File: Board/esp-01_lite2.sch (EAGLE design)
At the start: 26 parts, among them IC1 TINY13-20SU

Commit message: update board
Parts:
- added R9: 3k3, rcl:R-EU_R0805
- R10: value 3k3 -> 0
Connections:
- net GND: now also R9.2
- net IN1: now also C6.2, R6.2; no longer C5.2, R1.2
- net IN2: now also C5.2, R1.2; no longer C6.2, R6.2
- net N$3: now also X3.-3; no longer X3.-1
- net N$4: now also X3.-1; no longer X3.-3
- net WAKE_UP: now also R9.1
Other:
- moved on the sheet: C5, R1, X3
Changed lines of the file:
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@@
 <?xml version="1.0" encoding="utf-8"?>
 <!DOCTYPE eagle SYSTEM "eagle.dtd">
-<eagle version="9.0.0">
+<eagle version="8.7.0">
 <drawing>
 <settings>
@@
 <setting verticaltext="up"/>
 </settings>
-<grid distance="0.01" unitdist="inch" unit="inch" style="lines" multiple="1" display="no" altdistance="0.01" altunitdist="inch" altunit="inch"/>
+<grid distance="0.1" unitdist="inch" unit="inch" style="lines" multiple="1" display="no" altdistance="0.01" altunitdist="inch" altunit="inch"/>
 <layers>
 <layer number="1" name="Top" color="4" fill="1" visible="no" active="no"/>
@@
 <part name="GND3" library="supply1" deviceset="GND" device=""/>
 <part name="GND4" library="supply1" deviceset="GND" device=""/>
-<part name="R10" library="resistor" library_urn="urn:adsk.eagle:library:348" deviceset="R-EU_" device="M0805" package3d_urn="urn:adsk.eagle:package:26079/1" value="3k3"/>
+<part name="R10" library="resistor" library_urn="urn:adsk.eagle:library:348" deviceset="R-EU_" device="M0805" package3d_urn="urn:adsk.eagle:package:26079/1" value="0"/>
 <part name="GND6" library="supply1" deviceset="GND" device=""/>
 <part name="R11" library="rcl" deviceset="R-EU_" device="R0805" value="200">
@@
 <part name="X3" library="con-wago255" library_urn="urn:adsk.eagle:library:198" deviceset="233-104" device="" package3d_urn="urn:adsk.eagle:package:10915/1"/>
 <part name="U$2" library="MCP1700T-3302E_TT" deviceset="MCP1700T-3302E/TT" device=""/>
+<part name="R9" library="rcl" deviceset="R-EU_" device="R0805" value="3k3">
+<attribute name="OM" value="3k6"/>
+</part>
+<part name="GND2" library="supply1" deviceset="GND" device=""/>
 </parts>
 <sheets>
@@
 </instance>
 <instance part="R8" gate="G$1" x="120.904" y="56.896" rot="R270"/>
-<instance part="R1" gate="G$1" x="131.826" y="82.804" smashed="yes">
-<attribute name="NAME" x="130.556" y="84.3026" size="1.778" layer="95"/>
-<attribute name="VALUE" x="130.556" y="79.502" size="1.778" layer="96"/>
+<instance part="R1" gate="G$1" x="131.826" y="92.964" smashed="yes">
+<attribute name="NAME" x="130.556" y="94.4626" size="1.778" layer="95"/>
+<attribute name="VALUE" x="130.556" y="89.662" size="1.778" layer="96"/>
 </instance>
 <instance part="R6" gate="G$1" x="131.826" y="115.824" smashed="yes">
@@
 <attribute name="VALUE" x="130.556" y="112.522" size="1.778" layer="96"/>
 </instance>
-<instance part="C5" gate="G$1" x="136.906" y="92.964" smashed="yes">
-<attribute name="NAME" x="139.954" y="90.551" size="1.778" layer="95"/>
-<attribute name="VALUE" x="129.54" y="90.297" size="1.778" layer="96"/>
+<instance part="C5" gate="G$1" x="136.906" y="101.092" smashed="yes">
+<attribute name="NAME" x="139.954" y="98.679" size="1.778" layer="95"/>
+<attribute name="VALUE" x="129.54" y="98.425" size="1.778" layer="96"/>
 </instance>
 <instance part="C6" gate="G$1" x="136.906" y="108.204" smashed="yes" rot="R180">
@@
 </instance>
 <instance part="S2" gate="1" x="87.376" y="38.354"/>
-<instance part="X3" gate="G$1" x="99.314" y="106.68" rot="R180"/>
+<instance part="X3" gate="G$1" x="105.918" y="105.664" rot="R180"/>
 <instance part="U$2" gate="G$1" x="46.736" y="115.316" rot="R180"/>
+<instance part="R9" gate="G$1" x="42.164" y="26.162" smashed="yes" rot="R270">
+<attribute name="NAME" x="36.8046" y="24.384" size="1.778" layer="95"/>
+<attribute name="VALUE" x="36.576" y="27.178" size="1.778" layer="96"/>
+</instance>
+<instance part="GND2" gate="1" x="42.164" y="15.494"/>
 </instances>
 <busses>
@@
 <wire x1="150.876" y1="105.664" x2="150.876" y2="103.124" width="0.1524" layer="91"/>
 </segment>
+<segment>
+<pinref part="R9" gate="G$1" pin="2"/>
+<wire x1="42.164" y1="21.082" x2="42.164" y2="18.034" width="0.1524" layer="91"/>
+<pinref part="GND2" gate="1" pin="GND"/>
+</segment>
 </net>
 <net name="+3V3" class="0">
@@
 </segment>
 <segment>
+<pinref part="R1" gate="G$1" pin="2"/>
+<pinref part="C5" gate="G$1" pin="2"/>
+<wire x1="136.906" y1="96.012" x2="136.906" y2="92.964" width="0.1524" layer="91"/>
+<wire x1="136.906" y1="92.964" x2="146.05" y2="92.964" width="0.1524" layer="91"/>
+<junction x="136.906" y="92.964"/>
+<label x="146.812" y="92.71" size="1.778" layer="95"/>
+</segment>
+</net>
+<net name="IN1" class="0">
+<segment>
+<pinref part="IC1" gate="G$1" pin="PB3/PCINT3/CLKI/ADC3"/>
+<wire x1="128.778" y1="41.656" x2="112.268" y2="41.656" width="0.1524" layer="91"/>
+<label x="112.014" y="41.91" size="1.778" layer="95"/>
+</segment>
+<segment>
 <pinref part="R6" gate="G$1" pin="2"/>
 <pinref part="C6" gate="G$1" pin="2"/>
@@
 <wire x1="136.906" y1="115.824" x2="144.526" y2="115.824" width="0.1524" layer="91"/>
 <junction x="136.906" y="115.824"/>
-<label x="144.526" y="115.824" size="1.778" layer="95"/>
-</segment>
-</net>
-<net name="IN1" class="0">
-<segment>
-<pinref part="IC1" gate="G$1" pin="PB3/PCINT3/CLKI/ADC3"/>
-<wire x1="128.778" y1="41.656" x2="112.268" y2="41.656" width="0.1524" layer="91"/>
-<label x="112.014" y="41.91" size="1.778" layer="95"/>
-</segment>
-<segment>
-<pinref part="R1" gate="G$1" pin="2"/>
-<pinref part="C5" gate="G$1" pin="2"/>
-<wire x1="136.906" y1="87.884" x2="136.906" y2="82.804" width="0.1524" layer="91"/>
-<wire x1="136.906" y1="82.804" x2="144.526" y2="82.804" width="0.1524" layer="91"/>
-<junction x="136.906" y="82.804"/>
-<label x="144.526" y="82.804" size="1.778" layer="95"/>
+<label x="145.288" y="116.332" size="1.778" layer="95"/>
 </segment>
 </net>
@@
 <segment>
 <pinref part="C5" gate="G$1" pin="1"/>
-<wire x1="123.19" y1="95.504" x2="136.906" y2="95.504" width="0.1524" layer="91"/>
 <pinref part="C6" gate="G$1" pin="1"/>
 <wire x1="124.206" y1="105.664" x2="136.906" y2="105.664" width="0.1524" layer="91"/>
 <wire x1="139.192" y1="105.664" x2="136.906" y2="105.664" width="0.1524" layer="91"/>
 <junction x="136.906" y="105.664"/>
-<wire x1="136.906" y1="105.664" x2="136.906" y2="95.504" width="0.1524" layer="91"/>
-<junction x="136.906" y="95.504"/>
-<label x="137.668" y="99.06" size="1.778" layer="95"/>
+<wire x1="136.906" y1="105.664" x2="136.906" y2="103.632" width="0.1524" layer="91"/>
+<label x="120.904" y="103.124" size="1.778" layer="95"/>
 <pinref part="R10" gate="G$1" pin="1"/>
+<wire x1="124.206" y1="105.664" x2="124.206" y2="110.744" width="0.1524" layer="91"/>
+<wire x1="124.206" y1="110.744" x2="113.538" y2="110.744" width="0.1524" layer="91"/>
+<pinref part="X3" gate="G$1" pin="-4"/>
 <pinref part="X3" gate="G$1" pin="-2"/>
-<wire x1="123.19" y1="95.504" x2="123.19" y2="106.68" width="0.1524" layer="91"/>
-<wire x1="123.19" y1="106.68" x2="106.934" y2="106.68" width="0.1524" layer="91"/>
-<wire x1="124.206" y1="105.664" x2="124.206" y2="111.76" width="0.1524" layer="91"/>
-<wire x1="124.206" y1="111.76" x2="106.934" y2="111.76" width="0.1524" layer="91"/>
-<pinref part="X3" gate="G$1" pin="-4"/>
+<wire x1="124.206" y1="105.664" x2="113.538" y2="105.664" width="0.1524" layer="91"/>
+<junction x="124.206" y="105.664"/>
 </segment>
 <segment>
@@
 <segment>
 <pinref part="U$1" gate="G$1" pin="CH_PD"/>
-<wire x1="18.034" y1="46.736" x2="43.942" y2="46.736" width="0.1524" layer="91"/>
+<wire x1="18.034" y1="46.736" x2="42.164" y2="46.736" width="0.1524" layer="91"/>
 <label x="18.034" y="47.498" size="1.778" layer="95"/>
+<pinref part="R9" gate="G$1" pin="1"/>
+<wire x1="42.164" y1="46.736" x2="43.942" y2="46.736" width="0.1524" layer="91"/>
+<wire x1="42.164" y1="31.242" x2="42.164" y2="46.736" width="0.1524" layer="91"/>
+<junction x="42.164" y="46.736"/>
 </segment>
 </net>
@@
 <pinref part="R6" gate="G$1" pin="1"/>
 <wire x1="126.746" y1="115.824" x2="116.84" y2="115.824" width="0.1524" layer="91"/>
-<pinref part="X3" gate="G$1" pin="-1"/>
-<wire x1="106.934" y1="104.14" x2="116.84" y2="104.14" width="0.1524" layer="91"/>
-<wire x1="116.84" y1="104.14" x2="116.84" y2="115.824" width="0.1524" layer="91"/>
+<pinref part="X3" gate="G$1" pin="-3"/>
+<wire x1="113.538" y1="108.204" x2="116.84" y2="108.204" width="0.1524" layer="91"/>
+<wire x1="116.84" y1="108.204" x2="116.84" y2="115.824" width="0.1524" layer="91"/>
 </segment>
 </net>
@@
 </segment>
 </net>
-<net name="N$4" class="0">
-<segment>
-<wire x1="126.746" y1="91.44" x2="126.746" y2="82.804" width="0.1524" layer="91"/>
-<pinref part="R1" gate="G$1" pin="1"/>
-<pinref part="X3" gate="G$1" pin="-3"/>
-<wire x1="106.934" y1="109.22" x2="120.396" y2="109.22" width="0.1524" layer="91"/>
-<wire x1="120.396" y1="109.22" x2="120.396" y2="91.44" width="0.1524" layer="91"/>
-<wire x1="120.396" y1="91.44" x2="126.746" y2="91.44" width="0.1524" layer="91"/>
-</segment>
-</net>
 <net name="N$2" class="0">
 <segment>
@@
 </segment>
 </net>
+<net name="N$4" class="0">
+<segment>
+<pinref part="X3" gate="G$1" pin="-1"/>
+<wire x1="113.538" y1="103.124" x2="116.84" y2="103.124" width="0.1524" layer="91"/>
+<wire x1="116.84" y1="103.124" x2="116.84" y2="92.964" width="0.1524" layer="91"/>
+<pinref part="R1" gate="G$1" pin="1"/>
+<wire x1="116.84" y1="92.964" x2="126.746" y2="92.964" width="0.1524" layer="91"/>
+</segment>
+</net>

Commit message: board
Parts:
- R11, R4: value 200 -> 300
- R8: device rcl:R-EU_0204/5 -> rcl:R-EU_R0805
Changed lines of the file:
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@@
 <part name="+3V3" library="supply1" deviceset="+3V3" device=""/>
 <part name="+3V4" library="supply1" deviceset="+3V3" device=""/>
-<part name="R4" library="rcl" library_urn="urn:adsk.eagle:library:334" deviceset="R-EU_" device="0207/2V" package3d_urn="urn:adsk.eagle:package:23490/1" value="200">
+<part name="R4" library="rcl" library_urn="urn:adsk.eagle:library:334" deviceset="R-EU_" device="0207/2V" package3d_urn="urn:adsk.eagle:package:23490/1" value="300">
 <spice>
 <pinmapping spiceprefix="R">
@@
 <part name="LOG" library="pinhead" deviceset="PINHD-1X1" device="" value="LOG"/>
 <part name="+3V8" library="supply1" deviceset="+3V3" device=""/>
-<part name="R8" library="rcl" library_urn="urn:adsk.eagle:library:334" deviceset="R-EU_" device="0204/5" package3d_urn="urn:adsk.eagle:package:23488/1" value="3k3">
+<part name="R8" library="rcl" library_urn="urn:adsk.eagle:library:334" deviceset="R-EU_" device="R0805" package3d_urn="urn:adsk.eagle:package:23553/2" value="3k3">
 <spice>
 <pinmapping spiceprefix="C">
@@
 <part name="R10" library="resistor" library_urn="urn:adsk.eagle:library:348" deviceset="R-EU_" device="M0805" package3d_urn="urn:adsk.eagle:package:26079/1" value="0"/>
 <part name="GND6" library="supply1" deviceset="GND" device=""/>
-<part name="R11" library="rcl" deviceset="R-EU_" device="R0805" value="200">
+<part name="R11" library="rcl" deviceset="R-EU_" device="R0805" value="300">
 <attribute name="OM" value="3k6"/>
 </part>

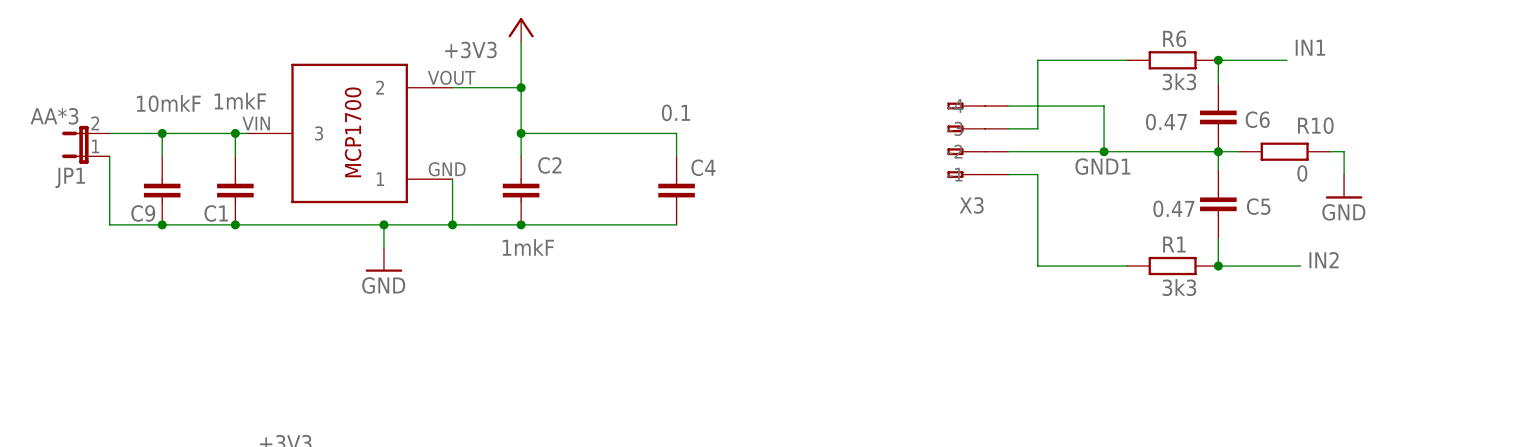
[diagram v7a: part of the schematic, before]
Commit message: v0.4 remove capacitor
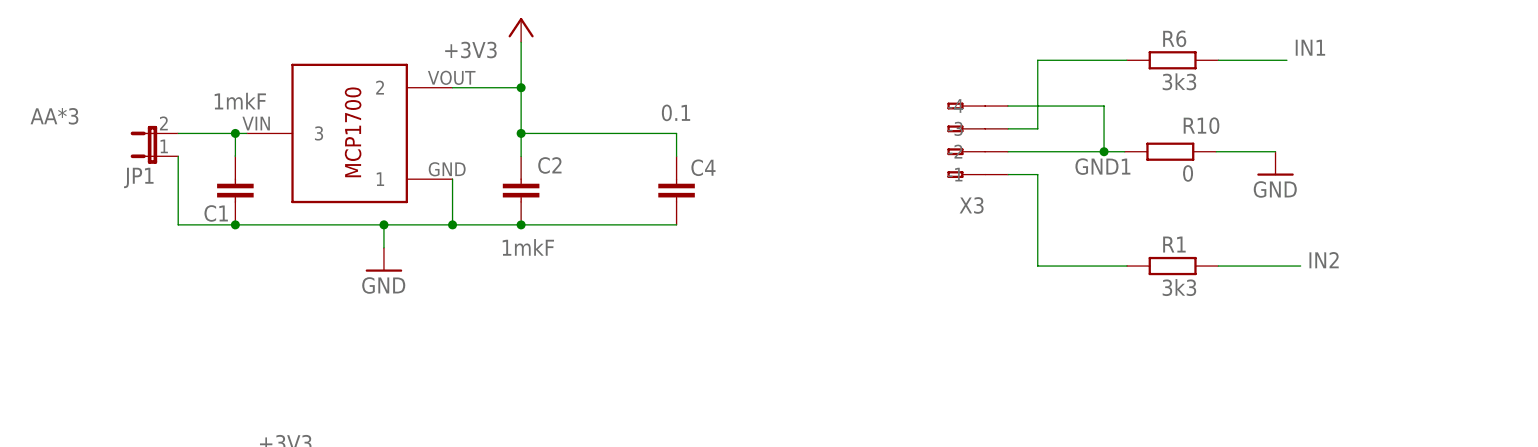
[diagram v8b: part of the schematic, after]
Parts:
- removed C5, C6: 0.47, resistor:C-EUC0805
- removed C9: 10mkF, rcl:C-EU025-030X050
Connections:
- net AA*3: no longer C9.1
- net GND: no longer C9.2
- net GND1: no longer C5.1, C6.1
- net IN1: no longer C6.2
- net IN2: no longer C5.2
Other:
- moved on the sheet: JP1, R10
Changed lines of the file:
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@@
 </part>
 <part name="R6" library="resistor" library_urn="urn:adsk.eagle:library:348" deviceset="R-EU_" device="M0805" package3d_urn="urn:adsk.eagle:package:26079/1" value="3k3"/>
-<part name="C5" library="resistor" library_urn="urn:adsk.eagle:library:348" deviceset="C-EU" device="C0805" package3d_urn="urn:adsk.eagle:package:26137/1" value="0.47">
-<attribute name="SPICEPREFIX" value="C"/>
-</part>
-<part name="C6" library="resistor" library_urn="urn:adsk.eagle:library:348" deviceset="C-EU" device="C0805" package3d_urn="urn:adsk.eagle:package:26137/1" value="0.47"/>
 <part name="C1" library="resistor" library_urn="urn:adsk.eagle:library:348" deviceset="C-EU" device="C0805" package3d_urn="urn:adsk.eagle:package:26137/1" value="1mkF"/>
 <part name="C2" library="resistor" library_urn="urn:adsk.eagle:library:348" deviceset="C-EU" device="C0805" package3d_urn="urn:adsk.eagle:package:26137/1" value="1mkF"/>
@@
 <attribute name="OM" value="3k6"/>
 </part>
-<part name="C9" library="rcl" library_urn="urn:adsk.eagle:library:334" deviceset="C-EU" device="025-030X050" package3d_urn="urn:adsk.eagle:package:23631/1" value="10mkF"/>
 <part name="GND3" library="supply1" deviceset="GND" device=""/>
 <part name="GND4" library="supply1" deviceset="GND" device=""/>
@@
 <attribute name="VALUE" x="130.556" y="112.522" size="1.778" layer="96"/>
 </instance>
-<instance part="C5" gate="G$1" x="136.906" y="101.092" smashed="yes">
-<attribute name="NAME" x="139.954" y="98.679" size="1.778" layer="95"/>
-<attribute name="VALUE" x="129.54" y="98.425" size="1.778" layer="96"/>
-</instance>
-<instance part="C6" gate="G$1" x="136.906" y="108.204" smashed="yes" rot="R180">
-<attribute name="NAME" x="142.748" y="110.109" size="1.778" layer="95" rot="R180"/>
-<attribute name="VALUE" x="133.604" y="109.855" size="1.778" layer="96" rot="R180"/>
-</instance>
 <instance part="C1" gate="G$1" x="27.686" y="102.616" smashed="yes">
 <attribute name="NAME" x="24.13" y="97.917" size="1.778" layer="95"/>
@@
 <attribute name="VALUE" x="41.656" y="89.916" size="1.778" layer="96"/>
 </instance>
-<instance part="JP1" gate="A" x="11.176" y="105.156" rot="R90"/>
+<instance part="JP1" gate="A" x="18.796" y="105.156" rot="R90"/>
 <instance part="+3V2" gate="G$1" x="59.436" y="120.396" smashed="yes">
 <attribute name="VALUE" x="56.896" y="117.856" size="1.778" layer="96" rot="R180"/>
@@
 <attribute name="VALUE" x="26.416" y="62.738" size="1.778" layer="96"/>
 </instance>
-<instance part="C9" gate="G$1" x="19.558" y="102.616" smashed="yes">
-<attribute name="NAME" x="16.002" y="97.917" size="1.778" layer="95"/>
-<attribute name="VALUE" x="16.51" y="110.109" size="1.778" layer="96"/>
-</instance>
 <instance part="GND3" gate="1" x="12.446" y="14.732"/>
 <instance part="GND4" gate="1" x="120.904" y="22.606"/>
-<instance part="R10" gate="G$1" x="144.272" y="105.664" smashed="yes">
-<attribute name="NAME" x="145.542" y="107.6706" size="1.778" layer="95"/>
-<attribute name="VALUE" x="145.542" y="102.362" size="1.778" layer="96"/>
-</instance>
-<instance part="GND6" gate="1" x="150.876" y="100.584"/>
+<instance part="R10" gate="G$1" x="131.572" y="105.664" smashed="yes">
+<attribute name="NAME" x="132.842" y="107.6706" size="1.778" layer="95"/>
+<attribute name="VALUE" x="132.842" y="102.362" size="1.778" layer="96"/>
+</instance>
+<instance part="GND6" gate="1" x="143.256" y="103.124"/>
 <instance part="R11" gate="G$1" x="87.376" y="26.67" smashed="yes" rot="R270">
 <attribute name="NAME" x="81.2546" y="26.67" size="1.778" layer="95"/>
@@
 <wire x1="44.196" y1="97.536" x2="27.686" y2="97.536" width="0.1524" layer="91"/>
 <pinref part="JP1" gate="A" pin="1"/>
-<wire x1="13.716" y1="105.156" x2="13.716" y2="97.536" width="0.1524" layer="91"/>
-<wire x1="27.686" y1="97.536" x2="19.558" y2="97.536" width="0.1524" layer="91"/>
-<pinref part="C9" gate="G$1" pin="2"/>
-<wire x1="19.558" y1="97.536" x2="13.716" y2="97.536" width="0.1524" layer="91"/>
-<junction x="19.558" y="97.536"/>
+<wire x1="21.336" y1="105.156" x2="21.336" y2="97.536" width="0.1524" layer="91"/>
+<wire x1="27.686" y1="97.536" x2="21.336" y2="97.536" width="0.1524" layer="91"/>
 <junction x="27.686" y="97.536"/>
 <pinref part="C4" gate="G$1" pin="2"/>
@@
 <segment>
 <pinref part="R10" gate="G$1" pin="2"/>
-<wire x1="149.352" y1="105.664" x2="150.876" y2="105.664" width="0.1524" layer="91"/>
+<wire x1="136.652" y1="105.664" x2="143.256" y2="105.664" width="0.1524" layer="91"/>
 <pinref part="GND6" gate="1" pin="GND"/>
-<wire x1="150.876" y1="105.664" x2="150.876" y2="103.124" width="0.1524" layer="91"/>
 </segment>
 <segment>
@@
 <segment>
 <pinref part="R1" gate="G$1" pin="2"/>
-<pinref part="C5" gate="G$1" pin="2"/>
-<wire x1="136.906" y1="96.012" x2="136.906" y2="92.964" width="0.1524" layer="91"/>
 <wire x1="136.906" y1="92.964" x2="146.05" y2="92.964" width="0.1524" layer="91"/>
-<junction x="136.906" y="92.964"/>
 <label x="146.812" y="92.71" size="1.778" layer="95"/>
 </segment>
@@
 <segment>
 <pinref part="R6" gate="G$1" pin="2"/>
-<pinref part="C6" gate="G$1" pin="2"/>
-<wire x1="136.906" y1="113.284" x2="136.906" y2="115.824" width="0.1524" layer="91"/>
 <wire x1="136.906" y1="115.824" x2="144.526" y2="115.824" width="0.1524" layer="91"/>
-<junction x="136.906" y="115.824"/>
 <label x="145.288" y="116.332" size="1.778" layer="95"/>
 </segment>
@@
 <net name="GND1" class="0">
 <segment>
-<pinref part="C5" gate="G$1" pin="1"/>
-<pinref part="C6" gate="G$1" pin="1"/>
-<wire x1="124.206" y1="105.664" x2="136.906" y2="105.664" width="0.1524" layer="91"/>
-<wire x1="139.192" y1="105.664" x2="136.906" y2="105.664" width="0.1524" layer="91"/>
-<junction x="136.906" y="105.664"/>
-<wire x1="136.906" y1="105.664" x2="136.906" y2="103.632" width="0.1524" layer="91"/>
+<wire x1="124.206" y1="105.664" x2="126.492" y2="105.664" width="0.1524" layer="91"/>
 <label x="120.904" y="103.124" size="1.778" layer="95"/>
 <pinref part="R10" gate="G$1" pin="1"/>
@@
 <segment>
 <pinref part="JP1" gate="A" pin="2"/>
-<wire x1="13.716" y1="107.696" x2="19.558" y2="107.696" width="0.1524" layer="91"/>
 <label x="10.414" y="110.49" size="1.778" layer="95" rot="R180"/>
 <pinref part="C1" gate="G$1" pin="1"/>
-<wire x1="19.558" y1="107.696" x2="27.686" y2="107.696" width="0.1524" layer="91"/>
+<wire x1="21.336" y1="107.696" x2="27.686" y2="107.696" width="0.1524" layer="91"/>
 <wire x1="27.686" y1="107.696" x2="28.956" y2="107.696" width="0.1524" layer="91"/>
 <wire x1="27.686" y1="105.156" x2="27.686" y2="107.696" width="0.1524" layer="91"/>
 <junction x="27.686" y="107.696"/>
-<pinref part="C9" gate="G$1" pin="1"/>
-<wire x1="19.558" y1="105.156" x2="19.558" y2="107.696" width="0.1524" layer="91"/>
-<junction x="19.558" y="107.696"/>
 <pinref part="U$2" gate="G$1" pin="3"/>
 </segment>
